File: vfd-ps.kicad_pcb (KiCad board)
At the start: 2 copper layers, 58 x 45 mm, 51 parts, among them J1 Conn_01x04, J2 Conn_01x04, J3 Conn_01x04, U1 TPS54360DDA, U2 LM4871

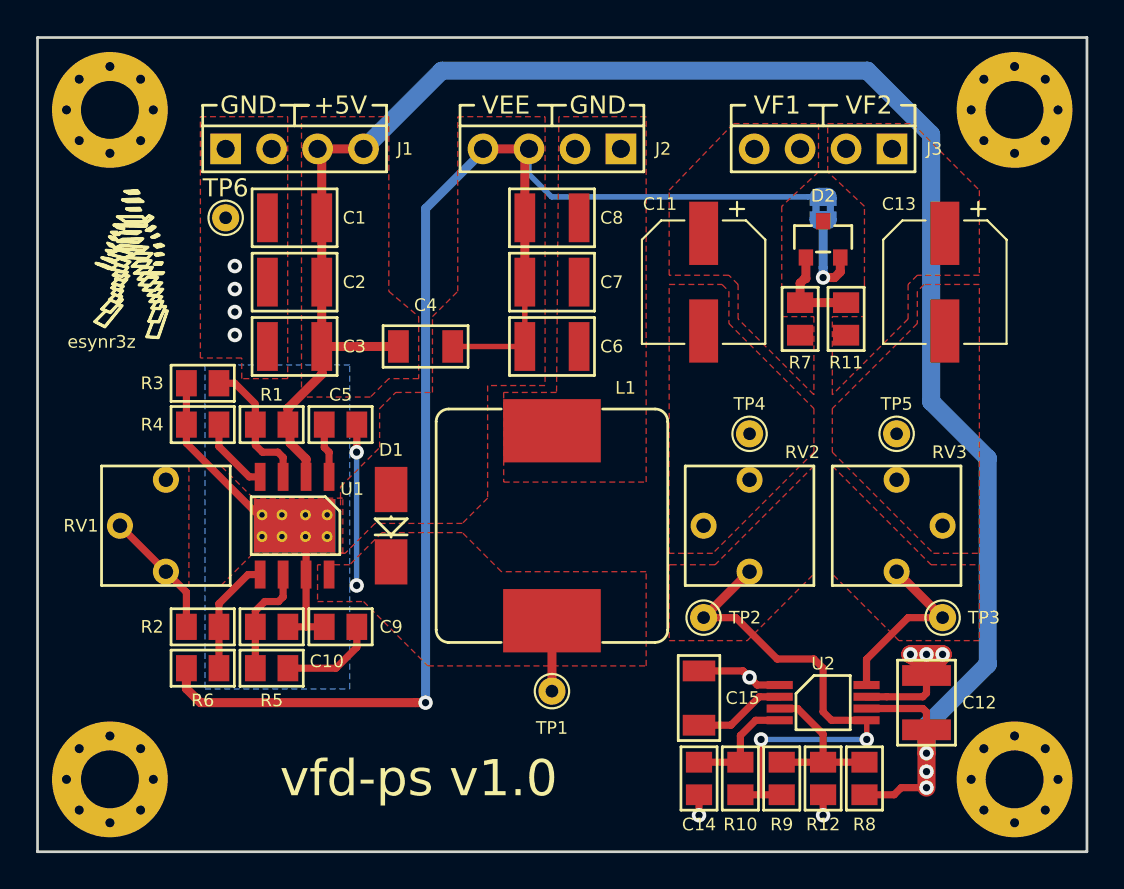
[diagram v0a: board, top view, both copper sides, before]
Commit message: Make project portable
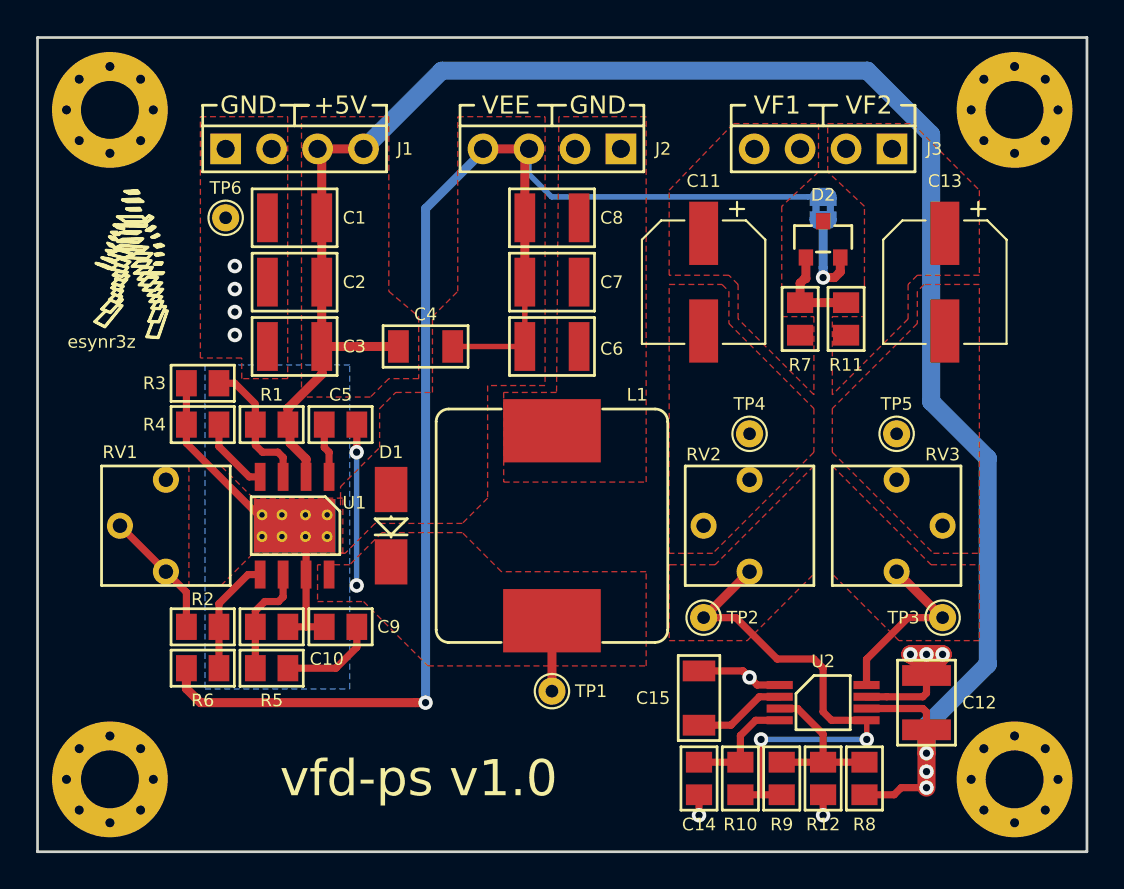
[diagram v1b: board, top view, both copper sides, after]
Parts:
- C1, C12, C2, C3, C6, C7, C8: footprint esynr3z_Capacitor:C_1210 -> lib_fp:C_1210
- C10, C14, C5, C9: footprint esynr3z_Capacitor:C_0805 -> lib_fp:C_0805
- C11, C13: footprint esynr3z_Capacitor:CP_Elec_6.3x7.7 -> lib_fp:CP_Elec_6.3x7.7
- C15, C4: footprint esynr3z_Capacitor:C_1206 -> lib_fp:C_1206
- D1: footprint esynr3z_Diode:SMA -> lib_fp:SMA
- D2: footprint esynr3z_SOT:SOT-23 -> lib_fp:SOT-23
- G***: footprint esynr3z_Symbol:iv18_draw -> fp_lib:iv18_draw
- G***: footprint esynr3z_Symbol:esynr3z_logo_4.5x8.4mm_Silk -> fp_lib:esynr3z_logo_4.5x8.4mm_Silk
- J1, J2, J3: footprint esynr3z_Connector:PinHeader_1x04_P2.54mm_Vertical -> lib_fp:PinHeader_1x04_P2.54mm_Vertical
- JP1: footprint esynr3z_Jumper:SolderJumper-2_P1.3mm_Bridged2Bar_RoundedPad1.0x1.5mm -> lib_fp:SolderJumper-2_P1.3mm_Bridged2Bar_RoundedPad1.0x1.5mm
- L1: footprint esynr3z_Inductor:Sumida_CDRH127 -> lib_fp:Sumida_CDRH127
- R1, R10, R11, R12, R2, R3, R4, R5, R6, R7, R8, R9: footprint esynr3z_Resistor:R_0805 -> lib_fp:R_0805
- REF** (x4): footprint MountingHole:MountingHole_3.2mm_M3_Pad_Via -> fp_lib:MountingHole_3.2mm_M3_Pad_Via
- RV1, RV2, RV3: footprint esynr3z_Potentiometer:Bourns_3362P -> lib_fp:Bourns_3362P
- TP1, TP2, TP3, TP4, TP5, TP6: footprint esynr3z_TestPoint:TestPoint_THTPad_D1.5mm_Drill0.7mm -> lib_fp:TestPoint_THTPad_D1.5mm_Drill0.7mm
- U1: footprint esynr3z_SO:TI_SO-PowerPAD-8_ThermalVias -> lib_fp:TI_SO-PowerPAD-8_ThermalVias
- U2: footprint esynr3z_SO:VSSOP-8_3.0x3.0mm_P0.65mm -> lib_fp:VSSOP-8_3.0x3.0mm_P0.65mm

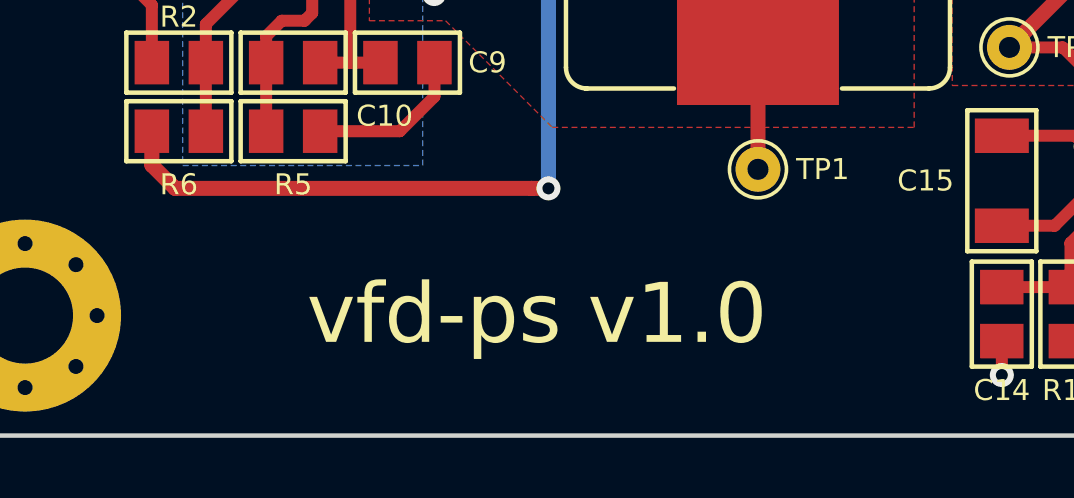
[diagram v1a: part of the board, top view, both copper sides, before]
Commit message: Update revision numbering
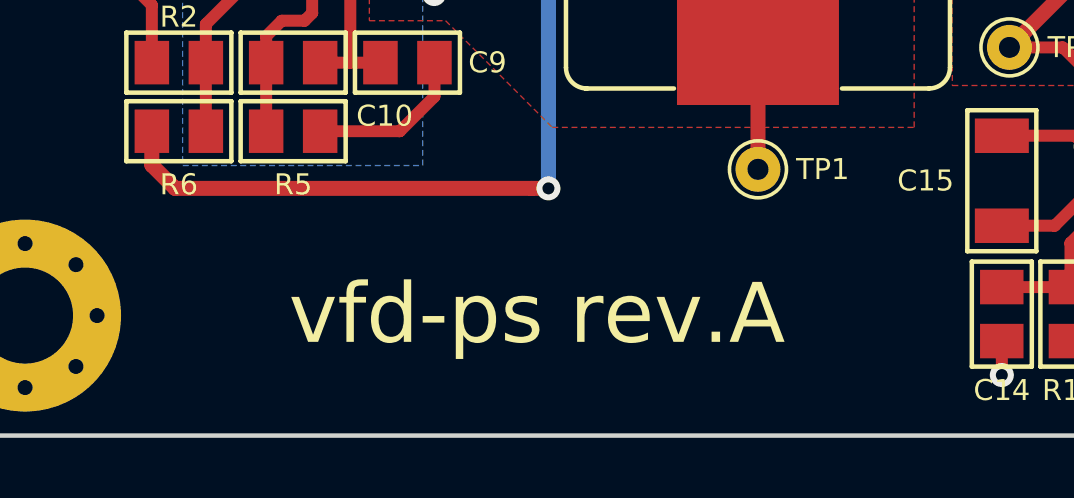
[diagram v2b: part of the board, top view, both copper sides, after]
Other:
- board text added: "vfd-ps rev.A"
- board text removed: "vfd-ps v1.0"
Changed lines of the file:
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@@
   (title_block
     (title "VFD power supply and filament driver")
-    (rev v1.0)
+    (rev A)
   )
   (layers
@@
   (gr_line (start 137.287 78.74) (end 136.525 78.74) (layer F.SilkS) (width 0.15))
   (gr_line (start 137.287 79.883) (end 137.287 78.74) (layer F.SilkS) (width 0.15))
-  (gr_text "vfd-ps v1.0" (at 139.065 115.951) (layer F.SilkS)
+  (gr_text "vfd-ps rev.A" (at 139.065 115.951) (layer F.SilkS)
     (effects (font (size 2 2) (thickness 0.4)))
   )
